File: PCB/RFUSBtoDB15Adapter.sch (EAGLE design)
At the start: 7 parts, among them J2 AVR_SPI_PROG_3X2NS

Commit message: New PCB
PCB updated
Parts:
- added C1: 0.1uf, Wurth_Elektronik_Passive_Capacitors_rev18b:WCAP-CSGP_0805_885012006082_REFLOW
- added C2: 10uF, SparkFun-Capacitors:10UF-POLAR-EIA3216-16V-10%(TANT)
- added IC1: S-816A40AMC-BAPT2U, S-816A40AMC-BAPT2U:S-816A40AMC-BAPT2U
- added JP2: (no value), pinhead:PINHD-1X1
- added LED: (no value), adafruit:LED3MM
- added PEM1, PEM2, PEM3, PEM4: KF2-M2, penn-engineering:KF2-M2
- added Q2: 2SA1213-Y(TE12L,F), 2SA1213YTE12LF:2SA1213-Y(TE12L,F)
- added R1: 33Ω, eagle-ltspice:R
- added SJ1, SJ2, SJ3: (no value), jumper:SJ
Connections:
- new net 5VREG: 3.3V.VIN, C1.1, C2.+, IC1.ON/OFF, IC1.VOUT, JP1.1, Q2.COLLECTOR, R1.2, SJ1.2, SJ3.1, SJ3.2
- new net BASE: IC1.EXT, Q2.BASE
- new net VBUS: C1.2, JP2.1, R1.1
- net 5VSG: now also IC1.VIN, Q2.EMITTER, SJ1.1, SJ2.1, SJ2.2; no longer 3.3V.VIN, J2.2, JP1.1
- net GND: now also C2.-, IC1.VSS
- net VCCIN: now also J2.2
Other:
- note added: "IF USING A 5V ARDUINO, FEED RAW (VCCIN) PIN WITH 3.3V FROM THE REGULATOR (REG1117)."
- note added: "THE 5V REGULATOR (IC1) WILL PROTECT THE VCC LINE FROM A POSSIBLE BAD PSU VOLTAGE, IF YOU DON'T NEED, JUST JUMPER SJ1."
- note removed: "IF USING A 5V ARDUINO, FEED RAW WITH 3.3V FROM THE REGULATOR."
- moved on the sheet: 3.3V, ARDUINO-ATMEGA328P, DB15OUT, J1, J2, JP1, JP3

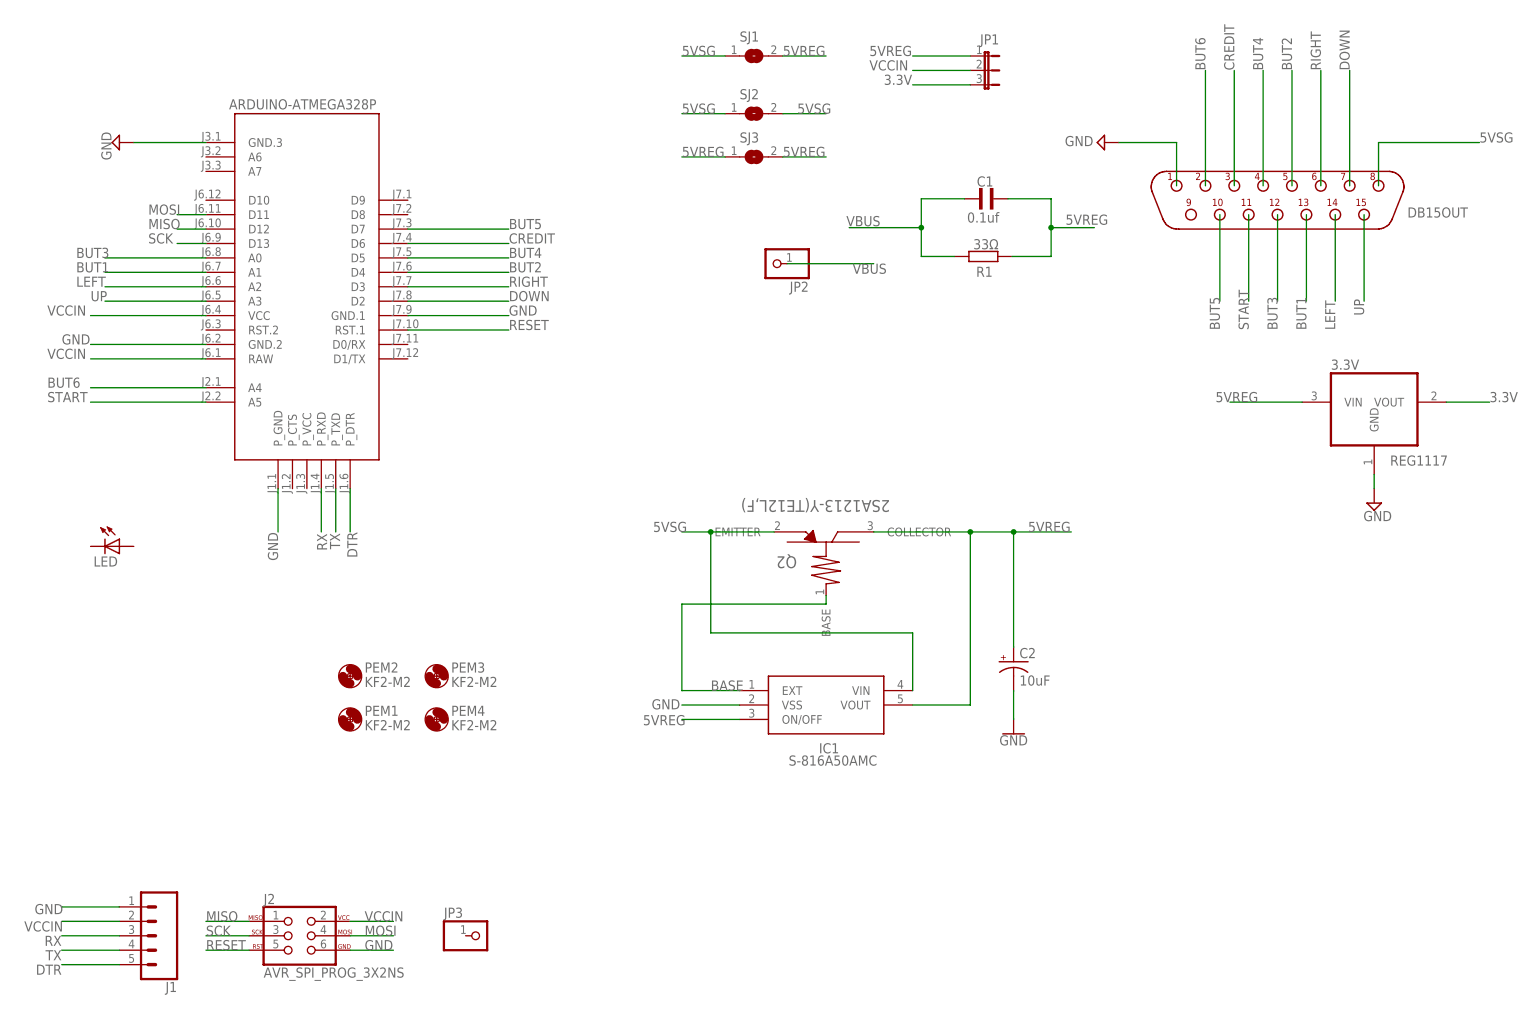
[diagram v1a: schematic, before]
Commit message: Updates
Schematic, PCB and code updates.
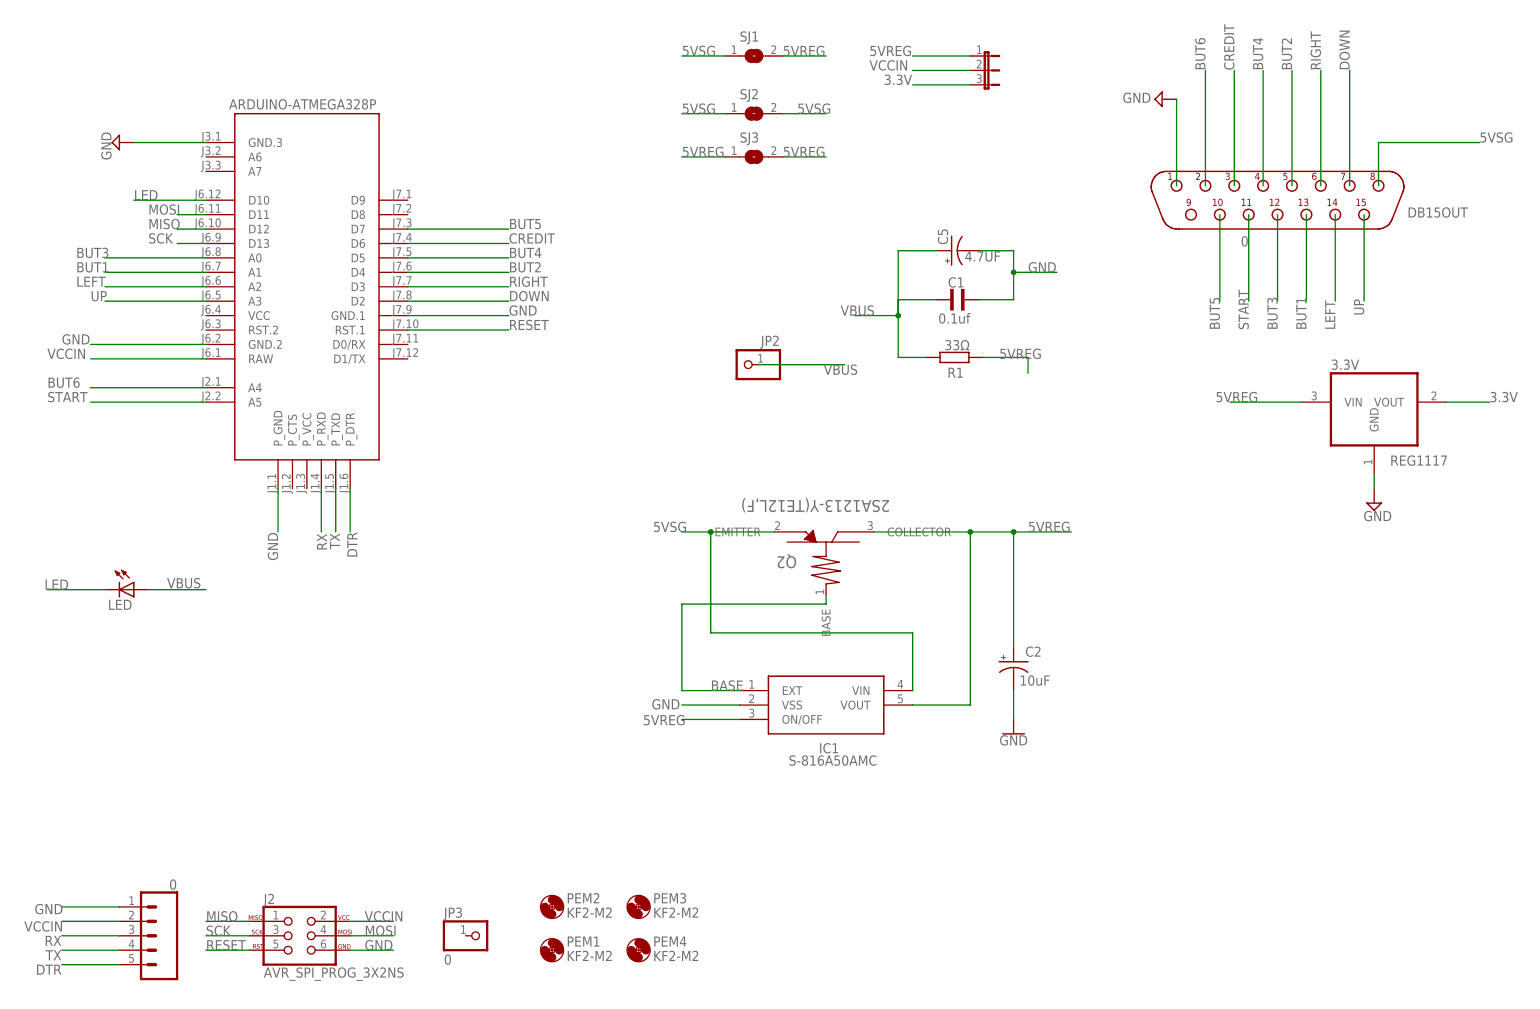
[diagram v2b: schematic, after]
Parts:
- added C5: 4.7UF, resistor:CPOL-USB/3528-21W
- DB15OUT, J1, JP3: value (none) -> 0
- JP2: value (none) -> JP2
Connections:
- new net LED: ARDUINO-ATMEGA328P.D10, LED.C
- net 5VREG: no longer C1.1
- net GND: now also C1.1, C5.-
- net VBUS: now also C5.+, LED.A
- net VCCIN: no longer ARDUINO-ATMEGA328P.VCC
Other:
- note added: "FEED USB HOST SHIELD MINI VBUS WITH JP2"
- moved on the sheet: C1, LED, PEM1, PEM2, PEM3, PEM4, R1

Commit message: PCB
Some changes
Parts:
- added LOGO1: OSHW-LOGOS, SparkFun-Aesthetics:OSHW-LOGOS
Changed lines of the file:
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@@
 <grid distance="0.1" unitdist="inch" unit="inch" style="lines" multiple="1" display="no" altdistance="0.01" altunitdist="inch" altunit="inch"/>
 <layers>
-<layer number="1" name="Top" color="4" fill="1" visible="yes" active="no"/>
-<layer number="2" name="Route2" color="16" fill="1" visible="yes" active="no"/>
-<layer number="3" name="Route3" color="17" fill="1" visible="yes" active="no"/>
-<layer number="4" name="Route4" color="18" fill="1" visible="yes" active="no"/>
-<layer number="5" name="Route5" color="19" fill="1" visible="yes" active="no"/>
-<layer number="6" name="Route6" color="25" fill="1" visible="yes" active="no"/>
-<layer number="7" name="Route7" color="26" fill="1" visible="yes" active="no"/>
-<layer number="8" name="Route8" color="27" fill="1" visible="yes" active="no"/>
-<layer number="9" name="Route9" color="28" fill="1" visible="yes" active="no"/>
-<layer number="10" name="Route10" color="29" fill="1" visible="yes" active="no"/>
-<layer number="11" name="Route11" color="30" fill="1" visible="yes" active="no"/>
-<layer number="12" name="Route12" color="20" fill="1" visible="yes" active="no"/>
-<layer number="13" name="Route13" color="21" fill="1" visible="yes" active="no"/>
-<layer number="14" name="Route14" color="22" fill="1" visible="yes" active="no"/>
-<layer number="15" name="Route15" color="23" fill="1" visible="yes" active="no"/>
-<layer number="16" name="Bottom" color="1" fill="1" visible="yes" active="no"/>
-<layer number="17" name="Pads" color="2" fill="1" visible="yes" active="no"/>
-<layer number="18" name="Vias" color="2" fill="1" visible="yes" active="no"/>
-<layer number="19" name="Unrouted" color="6" fill="1" visible="yes" active="no"/>
-<layer number="20" name="Dimension" color="24" fill="1" visible="yes" active="no"/>
-<layer number="21" name="tPlace" color="7" fill="1" visible="yes" active="no"/>
-<layer number="22" name="bPlace" color="7" fill="1" visible="yes" active="no"/>
-<layer number="23" name="tOrigins" color="15" fill="1" visible="yes" active="no"/>
-<layer number="24" name="bOrigins" color="15" fill="1" visible="yes" active="no"/>
-<layer number="25" name="tNames" color="7" fill="1" visible="yes" active="no"/>
-<layer number="26" name="bNames" color="7" fill="1" visible="yes" active="no"/>
-<layer number="27" name="tValues" color="7" fill="1" visible="yes" active="no"/>
-<layer number="28" name="bValues" color="7" fill="1" visible="yes" active="no"/>
+<layer number="1" name="Top" color="4" fill="1" visible="no" active="no"/>
+<layer number="2" name="Route2" color="16" fill="1" visible="no" active="no"/>
+<layer number="3" name="Route3" color="17" fill="1" visible="no" active="no"/>
+<layer number="4" name="Route4" color="18" fill="1" visible="no" active="no"/>
+<layer number="5" name="Route5" color="19" fill="1" visible="no" active="no"/>
+<layer number="6" name="Route6" color="25" fill="1" visible="no" active="no"/>
+<layer number="7" name="Route7" color="26" fill="1" visible="no" active="no"/>
+<layer number="8" name="Route8" color="27" fill="1" visible="no" active="no"/>
+<layer number="9" name="Route9" color="28" fill="1" visible="no" active="no"/>
+<layer number="10" name="Route10" color="29" fill="1" visible="no" active="no"/>
+<layer number="11" name="Route11" color="30" fill="1" visible="no" active="no"/>
+<layer number="12" name="Route12" color="20" fill="1" visible="no" active="no"/>
+<layer number="13" name="Route13" color="21" fill="1" visible="no" active="no"/>
+<layer number="14" name="Route14" color="22" fill="1" visible="no" active="no"/>
+<layer number="15" name="Route15" color="23" fill="1" visible="no" active="no"/>
+<layer number="16" name="Bottom" color="1" fill="1" visible="no" active="no"/>
+<layer number="17" name="Pads" color="2" fill="1" visible="no" active="no"/>
+<layer number="18" name="Vias" color="2" fill="1" visible="no" active="no"/>
+<layer number="19" name="Unrouted" color="6" fill="1" visible="no" active="no"/>
+<layer number="20" name="Dimension" color="24" fill="1" visible="no" active="no"/>
+<layer number="21" name="tPlace" color="7" fill="1" visible="no" active="no"/>
+<layer number="22" name="bPlace" color="7" fill="1" visible="no" active="no"/>
+<layer number="23" name="tOrigins" color="15" fill="1" visible="no" active="no"/>
+<layer number="24" name="bOrigins" color="15" fill="1" visible="no" active="no"/>
+<layer number="25" name="tNames" color="7" fill="1" visible="no" active="no"/>
+<layer number="26" name="bNames" color="7" fill="1" visible="no" active="no"/>
+<layer number="27" name="tValues" color="7" fill="1" visible="no" active="no"/>
+<layer number="28" name="bValues" color="7" fill="1" visible="no" active="no"/>
 <layer number="29" name="tStop" color="7" fill="3" visible="no" active="no"/>
 <layer number="30" name="bStop" color="7" fill="6" visible="no" active="no"/>
@@
 <layer number="35" name="tGlue" color="7" fill="4" visible="no" active="no"/>
 <layer number="36" name="bGlue" color="7" fill="5" visible="no" active="no"/>
-<layer number="37" name="tTest" color="7" fill="1" visible="yes" active="no"/>
-<layer number="38" name="bTest" color="7" fill="1" visible="yes" active="no"/>
+<layer number="37" name="tTest" color="7" fill="1" visible="no" active="no"/>
+<layer number="38" name="bTest" color="7" fill="1" visible="no" active="no"/>
 <layer number="39" name="tKeepout" color="4" fill="11" visible="no" active="no"/>
 <layer number="40" name="bKeepout" color="1" fill="11" visible="no" active="no"/>
@@
 <layer number="44" name="Drills" color="7" fill="1" visible="no" active="no"/>
 <layer number="45" name="Holes" color="7" fill="1" visible="no" active="no"/>
-<layer number="46" name="Milling" color="3" fill="1" visible="yes" active="no"/>
-<layer number="47" name="Measures" color="7" fill="1" visible="yes" active="no"/>
-<layer number="48" name="Document" color="7" fill="1" visible="yes" active="no"/>
-<layer number="49" name="Reference" color="7" fill="1" visible="yes" active="no"/>
-<layer number="50" name="dxf" color="7" fill="1" visible="yes" active="no"/>
-<layer number="51" name="tDocu" color="7" fill="1" visible="yes" active="no"/>
-<layer number="52" name="bDocu" color="7" fill="1" visible="yes" active="no"/>
-<layer number="53" name="tGND_GNDA" color="7" fill="9" visible="yes" active="no"/>
-<layer number="54" name="bGND_GNDA" color="1" fill="9" visible="yes" active="no"/>
-<layer number="56" name="wert" color="7" fill="1" visible="yes" active="no"/>
-<layer number="57" name="tCAD" color="7" fill="1" visible="yes" active="no"/>
-<layer number="59" name="tCarbon" color="7" fill="1" visible="yes" active="no"/>
-<layer number="60" name="bCarbon" color="7" fill="1" visible="yes" active="no"/>
+<layer number="46" name="Milling" color="3" fill="1" visible="no" active="no"/>
+<layer number="47" name="Measures" color="7" fill="1" visible="no" active="no"/>
+<layer number="48" name="Document" color="7" fill="1" visible="no" active="no"/>
+<layer number="49" name="Reference" color="7" fill="1" visible="no" active="no"/>
+<layer number="50" name="dxf" color="7" fill="1" visible="no" active="no"/>
+<layer number="51" name="tDocu" color="7" fill="1" visible="no" active="no"/>
+<layer number="52" name="bDocu" color="7" fill="1" visible="no" active="no"/>
+<layer number="53" name="tGND_GNDA" color="7" fill="9" visible="no" active="no"/>
+<layer number="54" name="bGND_GNDA" color="1" fill="9" visible="no" active="no"/>
+<layer number="56" name="wert" color="7" fill="1" visible="no" active="no"/>
+<layer number="57" name="tCAD" color="7" fill="1" visible="no" active="no"/>
+<layer number="59" name="tCarbon" color="7" fill="1" visible="no" active="no"/>
+<layer number="60" name="bCarbon" color="7" fill="1" visible="no" active="no"/>
 <layer number="88" name="SimResults" color="9" fill="1" visible="yes" active="yes"/>
 <layer number="89" name="SimProbes" color="9" fill="1" visible="yes" active="yes"/>
@@
 <part name="PEM4" library="penn-engineering" deviceset="KF2-" device="M2"/>
 <part name="C5" library="resistor" library_urn="urn:adsk.eagle:library:348" deviceset="CPOL-US" device="B/3528-21W" package3d_urn="urn:adsk.eagle:package:23411/1" value="4.7UF"/>
+<part name="LOGO1" library="SparkFun-Aesthetics" library_urn="urn:adsk.eagle:library:507" deviceset="OSHW-LOGO" device="S" package3d_urn="urn:adsk.eagle:package:37099/1"/>
 </parts>
 <sheets>
@@
 <attribute name="VALUE" x="11.684" y="75.565" size="1.778" layer="96"/>
 </instance>
+<instance part="LOGO1" gate="G$1" x="-142.24" y="-20.32" smashed="yes"/>
 </instances>
 <busses>

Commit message: PCB
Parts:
- removed JP3: 0, pinhead:PINHD-1X1
- added A4: 0, pinhead:PINHD-1X1
- added S1: RS032G05A3SM-SPST-MOMENTARY-SWSMD-1101NE, BeagleBone_Blue_R3:RS032G05A3SM-SPST-MOMENTARY-SWSMD-1101NE
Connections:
- net BUT6: now also A4.1
- net GND: now also S1.1; no longer ARDUINO-ATMEGA328P.GND.3
- net RESET: now also S1.2
- net START: now also ARDUINO-ATMEGA328P.GND.3
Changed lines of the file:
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@@
 <setting verticaltext="up"/>
 </settings>
-<grid distance="0.1" unitdist="inch" unit="inch" style="lines" multiple="1" display="no" altdistance="0.01" altunitdist="inch" altunit="inch"/>
+<grid distance="0.1" unitdist="inch" unit="inch" style="lines" multiple="1" display="yes" altdistance="0.01" altunitdist="inch" altunit="inch"/>
 <layers>
 <layer number="1" name="Top" color="4" fill="1" visible="no" active="no"/>
@@
 <part name="SUPPLY3" library="supply2" library_urn="urn:adsk.eagle:library:372" deviceset="GND" device=""/>
 <part name="SUPPLY5" library="supply2" library_urn="urn:adsk.eagle:library:372" deviceset="GND" device=""/>
-<part name="SUPPLY6" library="supply2" library_urn="urn:adsk.eagle:library:372" deviceset="GND" device=""/>
 <part name="FRAME1" library="SparkFun-Aesthetics" library_urn="urn:adsk.eagle:library:507" deviceset="FRAME-A4L" device="">
 <attribute name="CNAME" value="USB2DB15 adapter for Supergun/Neogeo"/>
@@
 <part name="J1" library="SparkFun-Connectors" library_urn="urn:adsk.eagle:library:513" deviceset="CONN_05" device="" package3d_urn="urn:adsk.eagle:package:38104/1" value="0"/>
 <part name="J2" library="SparkFun-Connectors" library_urn="urn:adsk.eagle:library:513" deviceset="AVR_SPI_PROG_3X2" device="NS" package3d_urn="urn:adsk.eagle:package:38013/1"/>
-<part name="JP3" library="pinhead" library_urn="urn:adsk.eagle:library:325" deviceset="PINHD-1X1" device="" package3d_urn="urn:adsk.eagle:package:22485/2" value="0"/>
+<part name="A4" library="pinhead" library_urn="urn:adsk.eagle:library:325" deviceset="PINHD-1X1" device="" package3d_urn="urn:adsk.eagle:package:22485/2" value="0"/>
 <part name="R1" library="eagle-ltspice" library_urn="urn:adsk.eagle:library:217" deviceset="R" device="" package3d_urn="urn:adsk.eagle:package:13300/1" value="33Ω"/>
 <part name="C1" library="Wurth_Elektronik_Passive_Capacitors_rev18b" library_urn="urn:adsk.eagle:library:7562178" deviceset="WCAP-CSGP_0805" device="_REFLOW" package3d_urn="urn:adsk.eagle:package:7562358/1" technology="_885012006082" value="0.1uf"/>
@@
 <part name="C5" library="resistor" library_urn="urn:adsk.eagle:library:348" deviceset="CPOL-US" device="B/3528-21W" package3d_urn="urn:adsk.eagle:package:23411/1" value="4.7UF"/>
 <part name="LOGO1" library="SparkFun-Aesthetics" library_urn="urn:adsk.eagle:library:507" deviceset="OSHW-LOGO" device="S" package3d_urn="urn:adsk.eagle:package:37099/1"/>
+<part name="S1" library="BeagleBone_Blue_R3" library_urn="urn:adsk.eagle:library:5828899" deviceset="RS032G05A3SM-SPST-MOMENTARY-SW" device="SMD-1101NE" package3d_urn="urn:adsk.eagle:package:5829833/3"/>
 </parts>
 <sheets>
@@
 <attribute name="VALUE" x="81.915" y="29.845" size="1.778" layer="96"/>
 </instance>
-<instance part="SUPPLY6" gate="GND" x="-137.16" y="96.52" smashed="yes" rot="R270">
-<attribute name="VALUE" x="-140.335" y="98.425" size="1.778" layer="96" rot="R270"/>
-</instance>
 <instance part="FRAME1" gate="G$1" x="-160.02" y="-58.42" smashed="yes">
 <attribute name="DRAWING_NAME" x="21.59" y="-46.99" size="2.54" layer="94" font="vector"/>
@@
 <attribute name="VALUE" x="-111.76" y="-50.546" size="1.778" layer="96" font="vector"/>
 </instance>
-<instance part="JP3" gate="G$1" x="-73.66" y="-43.18" smashed="yes">
-<attribute name="NAME" x="-80.01" y="-40.005" size="1.778" layer="95"/>
-<attribute name="VALUE" x="-80.01" y="-48.26" size="1.778" layer="96"/>
+<instance part="A4" gate="G$1" x="-101.6" y="-25.4" smashed="yes" rot="R90">
+<attribute name="NAME" x="-104.775" y="-31.75" size="1.778" layer="95" rot="R90"/>
 </instance>
 <instance part="R1" gate="G$1" x="9.906" y="58.674" smashed="yes">
@@
 </instance>
 <instance part="LOGO1" gate="G$1" x="-142.24" y="-20.32" smashed="yes"/>
+<instance part="S1" gate="G$1" x="-104.14" y="-2.54" smashed="yes">
+<attribute name="NAME" x="-106.68" y="0" size="1.778" layer="95"/>
+</instance>
 </instances>
 <busses>
@@
 <label x="-149.86" y="50.8" size="1.778" layer="95"/>
 </segment>
+<segment>
+<pinref part="ARDUINO-ATMEGA328P" gate="G$1" pin="GND.3"/>
+<wire x1="-121.92" y1="96.52" x2="-134.62" y2="96.52" width="0.1524" layer="91"/>
+<label x="-134.62" y="96.52" size="1.778" layer="95"/>
+</segment>
 </net>
 <net name="BUT4" class="0">
@@
 <label x="54.102" y="109.22" size="1.778" layer="95" rot="R90"/>
 </segment>
+<segment>
+<pinref part="A4" gate="G$1" pin="1"/>
+<wire x1="-101.6" y1="-27.94" x2="-116.84" y2="-27.94" width="0.1524" layer="91"/>
+<label x="-117.348" y="-27.178" size="1.778" layer="95"/>
+</segment>
 </net>
 <net name="GND" class="0">
@@
 <pinref part="3.3V" gate="G$1" pin="GND"/>
 <pinref part="SUPPLY5" gate="GND" pin="GND"/>
-</segment>
-<segment>
-<wire x1="-121.92" y1="96.52" x2="-134.62" y2="96.52" width="0.1524" layer="91"/>
-<pinref part="ARDUINO-ATMEGA328P" gate="G$1" pin="GND.3"/>
-<pinref part="SUPPLY6" gate="GND" pin="GND"/>
 </segment>
 <segment>
@@
 <pinref part="C5" gate="G$1" pin="-"/>
 </segment>
+<segment>
+<pinref part="S1" gate="G$1" pin="1"/>
+<wire x1="-109.22" y1="-2.54" x2="-121.92" y2="-2.54" width="0.1524" layer="91"/>
+<label x="-121.92" y="-2.54" size="1.778" layer="95"/>
+</segment>
 </net>
 <net name="5VSG" class="0">
@@
 <label x="-121.92" y="-45.72" size="1.778" layer="95"/>
 </segment>
-</net>
+<segment>
+<pinref part="S1" gate="G$1" pin="2"/>
+<wire x1="-99.06" y1="-2.54" x2="-86.36" y2="-2.54" width="0.1524" layer="91"/>
+<label x="-93.98" y="-2.54" size="1.778" layer="95"/>
+</segment>
+</net>
